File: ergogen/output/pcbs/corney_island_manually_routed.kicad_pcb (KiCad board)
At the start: 2 copper layers, 133.8 x 91.7 mm, 94 parts

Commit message: Add JLCPCB production number text
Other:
- board text added: "JLCJLCJLCJLC"
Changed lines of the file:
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@@
   (gr_arc (start 151.818892 49.918053) (mid 151.965339 49.564498) (end 152.318893 49.418054)
     (stroke (width 0.15) (type solid)) (layer "Edge.Cuts"))
+  (gr_text "JLCJLCJLCJLC" (at 213.22 59.64) (layer "F.SilkS")
+    (effects (font (size 1 1) (thickness 0.153)) (justify left bottom))
+  )
   (segment (start 219.658895 94.880053) (end 219.658893 96.690054) (width 0.2) (layer "F.Cu") (net 0))
   (segment (start 222.198892 94.88005) (end 222.198894 96.690054) (width 0.2) (layer "F.Cu") (net 0))

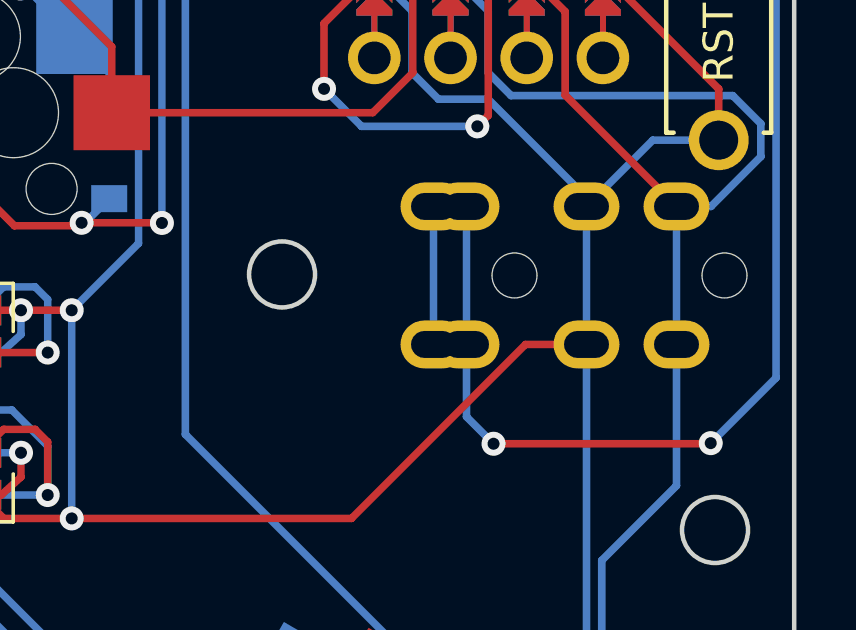
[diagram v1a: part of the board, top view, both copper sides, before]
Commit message: Fix pin 1 and 2 of the TRRS footprint
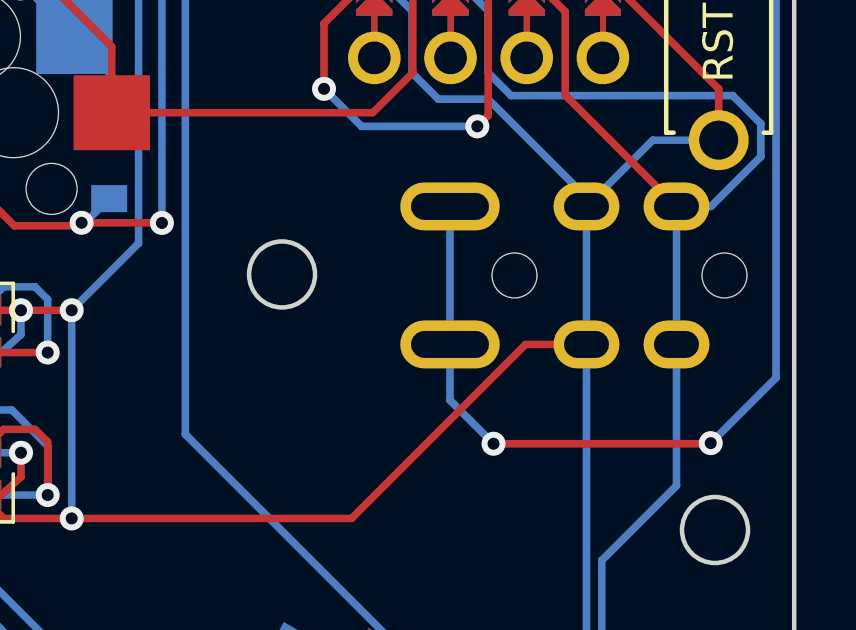
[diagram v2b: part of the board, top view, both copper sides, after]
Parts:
- TRRS1: footprint TRRS-PJ-320A-dual -> ceoloide:TRRS-PJ-320A-dual
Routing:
- net data: track 80.2 -> 75.9 mm
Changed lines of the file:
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@@
       (net 11 "ring_home"))
   )
-  (footprint "TRRS-PJ-320A-dual" (layer "F.Cu")
+  (footprint "ceoloide:TRRS-PJ-320A-dual" (layer "F.Cu")
     (at 227.848892 106.240052 -90)
     (attr through_hole)
@@
     (pad "" np_thru_hole circle (at -2.3 1.6) (size 1.5 1.5) (drill 1.5) (layers "*.Cu" "*.Mask"))
     (pad "" np_thru_hole circle (at -2.3 8.6) (size 1.5 1.5) (drill 1.5) (layers "*.Cu" "*.Mask"))
-    (pad "1" thru_hole oval (at -4.6 11.3 270) (size 1.6 2.2) (drill oval 0.9 1.5) (layers "*.Cu" "*.Mask")
+    (pad "1" thru_hole oval (at -4.6 10.75 270) (size 1.6 3.32) (drill oval 0.9 2.6) (layers "*.Cu" "*.Mask")
       (net 66 "data"))
-    (pad "1" thru_hole oval (at 0 11.3 270) (size 1.6 2.2) (drill oval 0.9 1.5) (layers "*.Cu" "*.Mask")
-      (net 66 "data"))
-    (pad "2" thru_hole oval (at -4.6 10.2 270) (size 1.6 2.2) (drill oval 0.9 1.5) (layers "*.Cu" "*.Mask")
-      (net 66 "data"))
-    (pad "2" thru_hole oval (at 0 10.2 270) (size 1.6 2.2) (drill oval 0.9 1.5) (layers "*.Cu" "*.Mask")
+    (pad "1" thru_hole oval (at 0 10.75 270) (size 1.6 3.32) (drill oval 0.9 2.6) (layers "*.Cu" "*.Mask")
       (net 66 "data"))
     (pad "3" thru_hole oval (at -4.6 6.2 270) (size 1.6 2.2) (drill oval 0.9 1.5) (layers "*.Cu" "*.Mask")
@@
   (via (at 225.79 109.53) (size 0.8) (drill 0.4) (layers "F.Cu" "B.Cu") (net 66))
   (segment (start 226.50374 65.38) (end 223.61 65.38) (width 0.254) (layer "B.Cu") (net 66))
-  (segment (start 217.648892 106.240052) (end 217.648892 108.648892) (width 0.254) (layer "B.Cu") (net 66))
   (segment (start 227.967927 107.352073) (end 227.967927 66.844187) (width 0.254) (layer "B.Cu") (net 66))
   (segment (start 222.048895 63.410053) (end 221.358896 63.410054) (width 0.25) (layer "B.Cu") (net 66))
-  (segment (start 217.648895 101.640053) (end 217.648896 106.240053) (width 0.25) (layer "B.Cu") (net 66))
   (segment (start 223.61 65.38) (end 223.217896 64.987896) (width 0.254) (layer "B.Cu") (net 66))
-  (segment (start 217.648892 108.648892) (end 218.55 109.55) (width 0.254) (layer "B.Cu") (net 66))
   (segment (start 222.778894 64.140052) (end 222.048895 63.410053) (width 0.25) (layer "B.Cu") (net 66))
   (segment (start 227.967927 66.844187) (end 226.50374 65.38) (width 0.254) (layer "B.Cu") (net 66))
   (segment (start 220.878895 63.890055) (end 215.428892 63.890055) (width 0.25) (layer "B.Cu") (net 66))
+  (segment (start 217.098892 108.098892) (end 218.55 109.55) (width 0.254) (layer "B.Cu") (net 66))
+  (segment (start 217.098892 101.640052) (end 217.098892 106.240052) (width 0.254) (layer "B.Cu") (net 66))
   (segment (start 225.79 109.53) (end 227.967927 107.352073) (width 0.254) (layer "B.Cu") (net 66))
   (segment (start 221.358896 63.410054) (end 220.878895 63.890055) (width 0.25) (layer "B.Cu") (net 66))
@@
   (segment (start 215.428892 63.890055) (end 215.178895 64.140051) (width 0.25) (layer "B.Cu") (net 66))
   (segment (start 223.218895 64.140053) (end 222.778894 64.140052) (width 0.25) (layer "B.Cu") (net 66))
-  (segment (start 216.548893 101.64005) (end 216.548892 106.240052) (width 0.25) (layer "B.Cu") (net 66))
+  (segment (start 217.098892 106.240052) (end 217.098892 108.098892) (width 0.254) (layer "B.Cu") (net 66))
   (segment (start 218.01 98.97) (end 218.373192 98.606808) (width 0.254) (layer "F.Cu") (net 67))
   (segment (start 214.575892 93.864053) (end 212.9 95.539945) (width 0.254) (layer "F.Cu") (net 67))

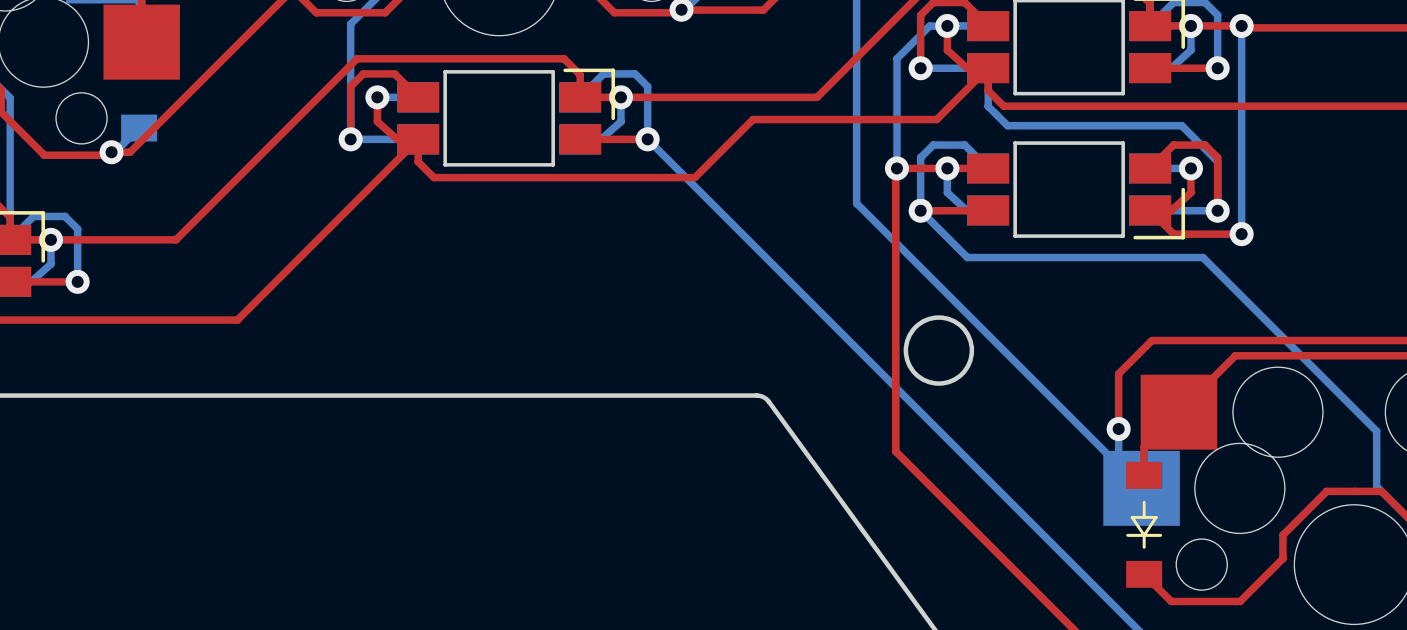
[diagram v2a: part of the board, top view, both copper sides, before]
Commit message: Add board name and version
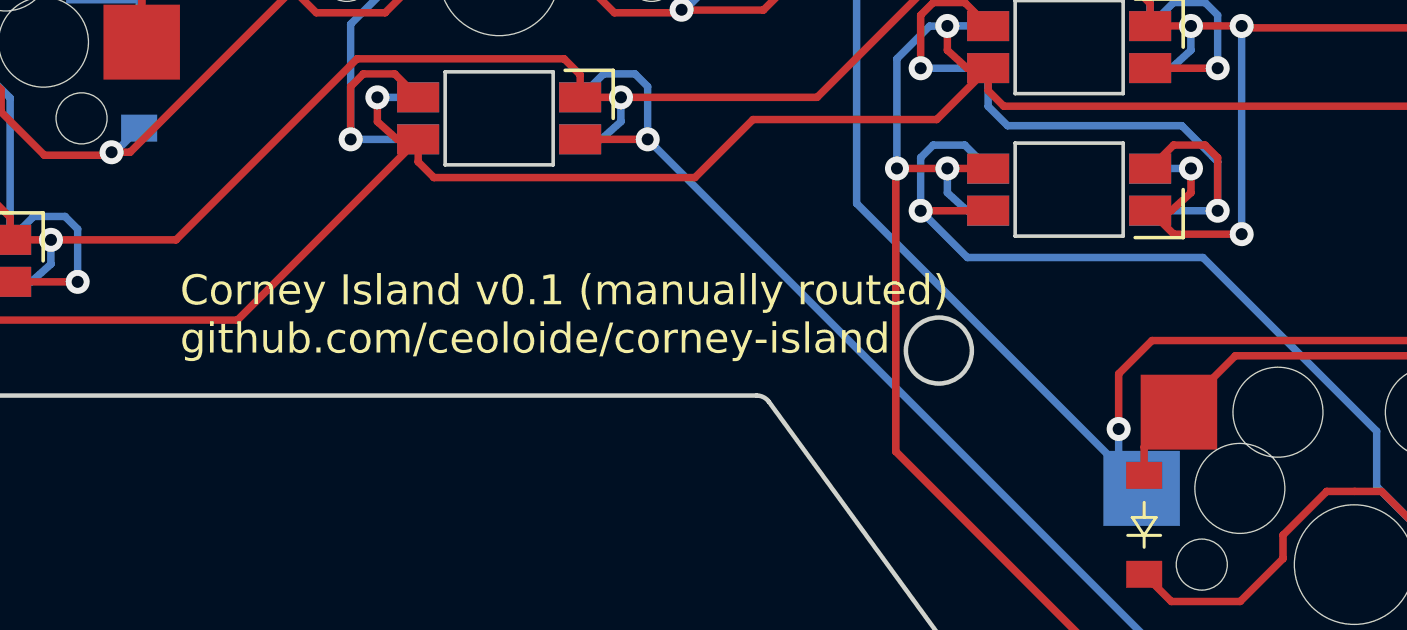
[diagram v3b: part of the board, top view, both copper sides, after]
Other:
- board text added: "Corney Island v0.1 (manually routed) github.com/ceoloide/corney-island"
